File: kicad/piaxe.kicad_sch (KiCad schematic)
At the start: 13 parts, among them J3 Barrel_Jack_Switch, M2 Fan_4pin

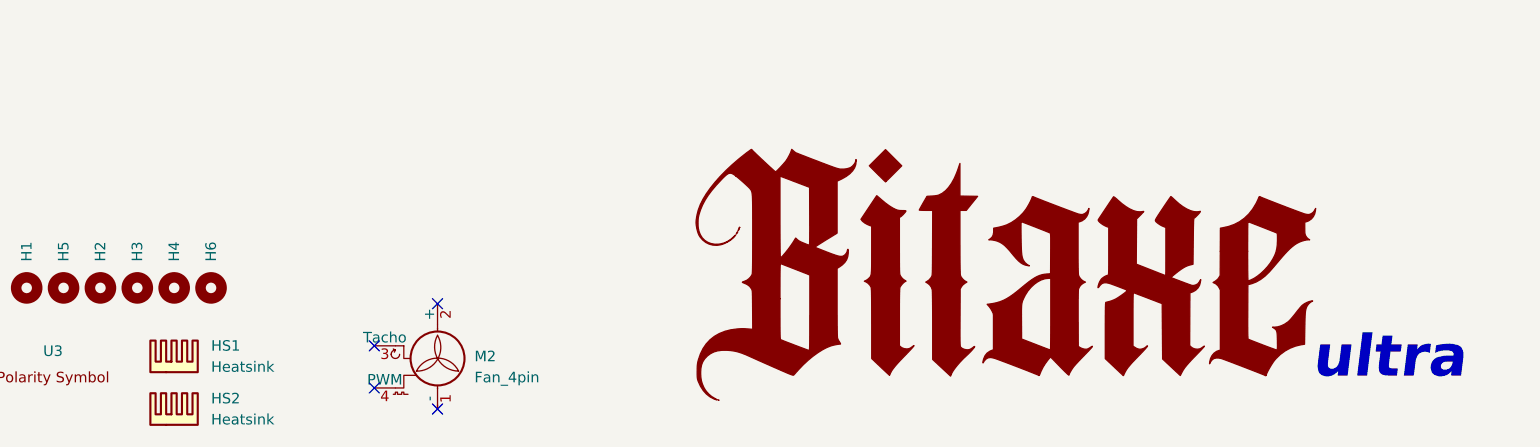
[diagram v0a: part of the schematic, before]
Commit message: fixed heatsink order number, updated BOM
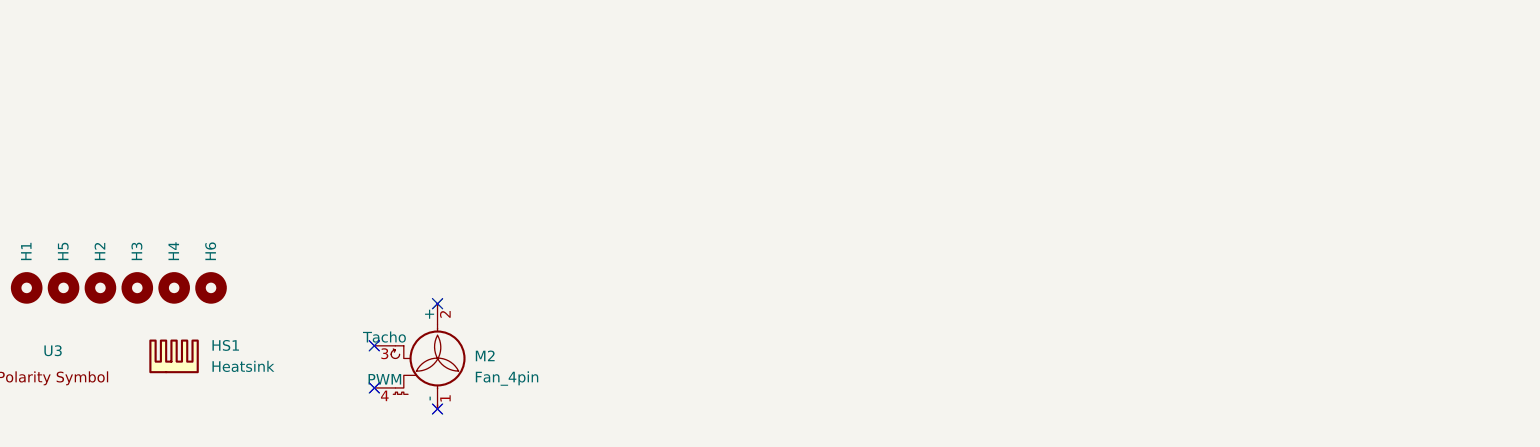
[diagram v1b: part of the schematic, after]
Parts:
- removed HS2: Heatsink, symbol Mechanical:Heatsink
- HS1: Manufacturer ATS-CPX040040025-184-C1-R0 -> ATS-CPX040040020-115-C1-R0; OrderNr ATS35997-ND -> ATS35987-ND
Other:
- note removed: "ultra"
- title: BM1366 bitaxe -> BM1366 PiAxe
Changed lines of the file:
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@@
   (paper "A")
   (title_block
-    (title "BM1366 bitaxe")
+    (title "BM1366 PiAxe")
     (date "2023-10-10")
     (rev "202")
@@
     (stroke (width 0) (type default))
   )
-  (text "ultra" (at 235.585 186.055 0)
-    (effects (font (size 5 5) (thickness 1) bold italic) (justify left bottom))
-  )
   (symbol (lib_id "Mechanical:MountingHole") (at 80.645 174.625 90) (unit 1)
     (in_bom yes) (on_board yes) (dnp no) (fields_autoplaced)
@@
     )
   )
-  (symbol (lib_id "bitaxe:LOGO") (at 197.485 173.99 0) (unit 1)
-    (in_bom yes) (on_board yes) (dnp no) (fields_autoplaced)
-    (property "Reference" "#G1" (at 197.485 146.4607 0)
-      (effects (font (size 1.27 1.27)) hide)
-    )
-    (property "Value" "LOGO" (at 197.485 201.5193 0)
-      (effects (font (size 1.27 1.27)) hide)
-    )
-    (property "Footprint" "" (at 197.485 173.99 0)
-      (effects (font (size 1.27 1.27)) hide)
-    )
-    (property "Datasheet" "" (at 197.485 173.99 0)
-      (effects (font (size 1.27 1.27)) hide)
-    )
-    (instances
-      (project "piaxe"
-        (path "/e63e39d7-6ac0-4ffd-8aa3-1841a4541b55"
-          (reference "#G1") (unit 1)
-        )
-      )
-    )
-  )
-  (symbol (lib_id "Mechanical:Heatsink") (at 98.425 191.135 0) (unit 1)
-    (in_bom yes) (on_board no) (dnp no) (fields_autoplaced)
-    (property "Reference" "HS2" (at 102.87 187.96 0)
-      (effects (font (size 1.27 1.27)) (justify left))
-    )
-    (property "Value" "Heatsink" (at 102.87 190.5 0)
-      (effects (font (size 1.27 1.27)) (justify left))
-    )
-    (property "Footprint" "" (at 98.7298 191.135 0)
-      (effects (font (size 1.27 1.27)) hide)
-    )
-    (property "Datasheet" "~" (at 98.7298 191.135 0)
-      (effects (font (size 1.27 1.27)) hide)
-    )
-    (property "Distributor" "D" (at 98.425 191.135 0)
-      (effects (font (size 1.27 1.27)) hide)
-    )
-    (property "Manufacturer" "ATS-FPX040040025-94-C2-R0" (at 98.425 191.135 0)
-      (effects (font (size 1.27 1.27)) hide)
-    )
-    (property "OrderNr" "ATS1674-ND" (at 98.425 191.135 0)
-      (effects (font (size 1.27 1.27)) hide)
-    )
-    (instances
-      (project "piaxe"
-        (path "/e63e39d7-6ac0-4ffd-8aa3-1841a4541b55"
-          (reference "HS2") (unit 1)
-        )
-      )
-    )
-  )
   (symbol (lib_id "bitaxe:polarity") (at 85.09 184.15 0) (unit 1)
     (in_bom no) (on_board yes) (dnp no) (fields_autoplaced)
@@
       (effects (font (size 1.27 1.27)) hide)
     )
-    (property "Manufacturer" "ATS-CPX040040025-184-C1-R0" (at 98.425 184.785 0)
-      (effects (font (size 1.27 1.27)) hide)
-    )
-    (property "OrderNr" "ATS35997-ND" (at 98.425 184.785 0)
-      (effects (font (size 1.27 1.27)) hide)
-    )
+    (property "Manufacturer" "ATS-CPX040040020-115-C1-R0" (at 98.425 184.785 0)
+      (effects (font (size 1.27 1.27)) hide)
+    )
+    (property "OrderNr" "ATS35987-ND" (at 98.425 184.785 0)
+      (effects (font (size 1.27 1.27)) hide)
+    )

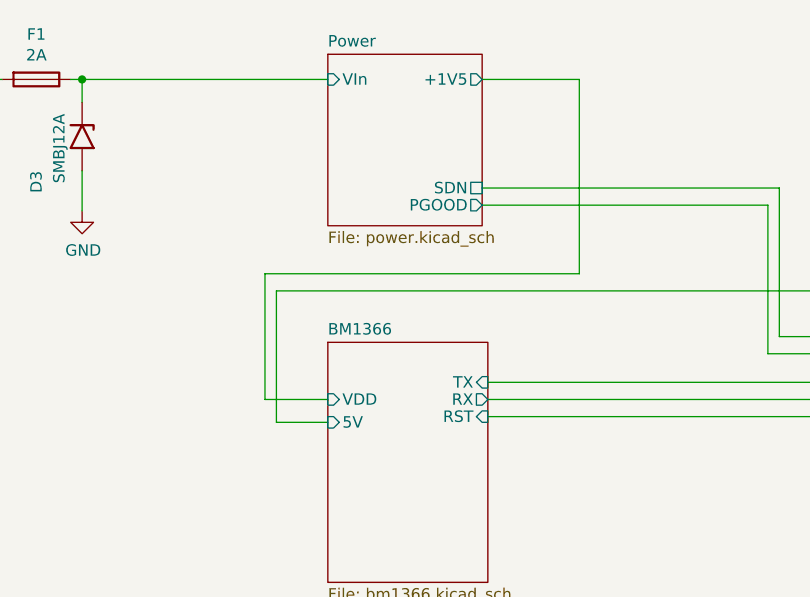
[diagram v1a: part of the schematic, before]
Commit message: fixed net labeling to 1.2V
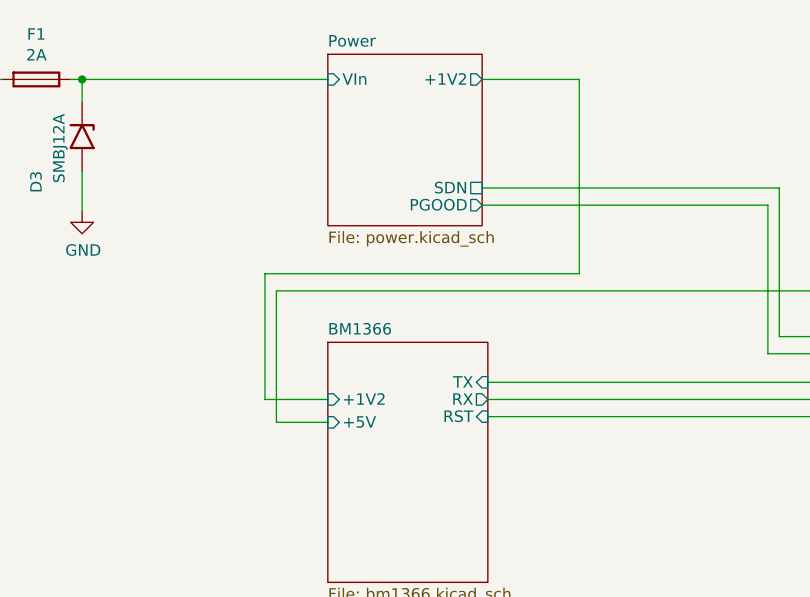
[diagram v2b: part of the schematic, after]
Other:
- sheet BM1366 ports: added +1V2, +5V; removed 5V, VDD
- sheet Power ports: added +1V2; removed +1V5
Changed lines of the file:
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@@
       (effects (font (size 1.27 1.27)) (justify right))
     )
-    (pin "5V" input (at 82.55 90.17 180)
+    (pin "+1V2" input (at 82.55 87.63 180)
       (effects (font (size 1.27 1.27)) (justify left))
     )
-    (pin "VDD" input (at 82.55 87.63 180)
+    (pin "+5V" input (at 82.55 90.17 180)
       (effects (font (size 1.27 1.27)) (justify left))
     )
@@
       (effects (font (size 1.27 1.27)) (justify right))
     )
-    (pin "+1V5" output (at 99.695 52.07 0)
-      (effects (font (size 1.27 1.27)) (justify right))
-    )
     (pin "SDN" passive (at 99.695 64.135 0)
       (effects (font (size 1.27 1.27)) (justify right))
@@
       (effects (font (size 1.27 1.27)) (justify left))
     )
+    (pin "+1V2" output (at 99.695 52.07 0)
+      (effects (font (size 1.27 1.27)) (justify right))
+    )
     (instances

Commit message: initial commit before replacing power supply
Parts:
- removed H1, H2, H3, H4, H5, H6: MountingHole, MountingHole:MountingHole_3.2mm_M3_DIN965_Pad, symbol Mechanical:MountingHole
- removed HS1: Heatsink, symbol Mechanical:Heatsink
- removed M2: Fan_4pin, symbol Motor:Fan_4pin
- renumbered U3 to U1
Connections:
- no-connect marks 4 -> 0
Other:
- sheet Power ports: added +0V8, +1V8, +3V3; removed none

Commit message: updated gerber, bom
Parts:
- F1: value 2A -> 5A; Manufacturer 0154002.DR -> 0154005.DR; OrderNr F1224CT-ND -> F1228CT-ND
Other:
- sheet Pi renamed STM32
- sheet BM1366 ports: added +0V8, +1V8, +3V3, RESET, RXD, TXD; removed +5V, RST, RX, TX
- sheet Power ports: added 1V2_PGOOD, 1V2_RUN; removed PGOOD, SDN
- sheet STM32 ports: added +3V3, 1V2_PGOOD, 1V2_RUN, RESET, RXD, TXD; removed +5V, BUCK_POWER_GOOD, BUCK_SHUTDOWN, MINER_RESET, MINER_RXD, MINER_TXD
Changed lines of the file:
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@@
     (rev "202")
   )
+  (junction (at 114.3 57.785) (diameter 0) (color 0 0 0 0)
+  )
   (junction (at 55.245 52.07) (diameter 0) (color 0 0 0 0)
   )
   (junction (at 43.815 57.15) (diameter 0) (color 0 0 0 0)
   )
-  (wire (pts (xy 110.49 73.66) (xy 75.565 73.66))
+  (wire (pts (xy 111.76 75.565) (xy 74.295 75.565))
+    (stroke (width 0) (type default))
+  )
+  (wire (pts (xy 74.295 75.565) (xy 74.295 89.535))
+    (stroke (width 0) (type default))
+  )
+  (wire (pts (xy 110.49 74.295) (xy 75.565 74.295))
     (stroke (width 0) (type default))
   )
@@
     (stroke (width 0) (type default))
   )
+  (wire (pts (xy 73.025 91.44) (xy 82.55 91.44))
+    (stroke (width 0) (type default))
+  )
   (wire (pts (xy 100.33 87.63) (xy 144.78 87.63))
     (stroke (width 0) (type default))
   )
+  (wire (pts (xy 73.025 76.835) (xy 73.025 91.44))
+    (stroke (width 0) (type default))
+  )
+  (wire (pts (xy 99.695 53.975) (xy 111.76 53.975))
+    (stroke (width 0) (type default))
+  )
   (wire (pts (xy 131.445 82.55) (xy 144.78 82.55))
     (stroke (width 0) (type default))
@@
     (stroke (width 0) (type default))
   )
+  (wire (pts (xy 71.755 78.105) (xy 71.755 93.345))
+    (stroke (width 0) (type default))
+  )
+  (wire (pts (xy 114.3 78.105) (xy 71.755 78.105))
+    (stroke (width 0) (type default))
+  )
   (wire (pts (xy 131.445 66.04) (xy 131.445 82.55))
     (stroke (width 0) (type default))
@@
     (stroke (width 0) (type default))
   )
-  (wire (pts (xy 110.49 52.07) (xy 110.49 73.66))
+  (wire (pts (xy 110.49 52.07) (xy 110.49 74.295))
     (stroke (width 0) (type default))
   )
@@
     (stroke (width 0) (type default))
   )
-  (wire (pts (xy 76.835 75.565) (xy 76.835 90.17))
+  (wire (pts (xy 71.755 93.345) (xy 82.55 93.345))
+    (stroke (width 0) (type default))
+  )
+  (wire (pts (xy 74.295 89.535) (xy 82.55 89.535))
+    (stroke (width 0) (type default))
+  )
+  (wire (pts (xy 144.78 78.74) (xy 133.985 78.74))
+    (stroke (width 0) (type default))
+  )
+  (wire (pts (xy 113.03 76.835) (xy 73.025 76.835))
+    (stroke (width 0) (type default))
+  )
+  (wire (pts (xy 133.985 78.74) (xy 133.985 57.785))
     (stroke (width 0) (type default))
   )
@@
     (stroke (width 0) (type default))
   )
-  (wire (pts (xy 144.78 75.565) (xy 76.835 75.565))
+  (wire (pts (xy 114.3 57.785) (xy 114.3 78.105))
     (stroke (width 0) (type default))
   )
@@
     (stroke (width 0) (type default))
   )
-  (wire (pts (xy 76.835 90.17) (xy 82.55 90.17))
-    (stroke (width 0) (type default))
-  )
   (wire (pts (xy 42.545 57.15) (xy 43.815 57.15))
     (stroke (width 0) (type default))
@@
     (stroke (width 0) (type default))
   )
+  (wire (pts (xy 113.03 55.88) (xy 113.03 76.835))
+    (stroke (width 0) (type default))
+  )
+  (wire (pts (xy 99.695 57.785) (xy 114.3 57.785))
+    (stroke (width 0) (type default))
+  )
+  (wire (pts (xy 133.985 57.785) (xy 114.3 57.785))
+    (stroke (width 0) (type default))
+  )
+  (wire (pts (xy 75.565 74.295) (xy 75.565 87.63))
+    (stroke (width 0) (type default))
+  )
+  (wire (pts (xy 99.695 55.88) (xy 113.03 55.88))
+    (stroke (width 0) (type default))
+  )
   (wire (pts (xy 100.33 85.725) (xy 144.78 85.725))
     (stroke (width 0) (type default))
@@
     (stroke (width 0) (type default))
   )
-  (wire (pts (xy 75.565 73.66) (xy 75.565 87.63))
-    (stroke (width 0) (type default))
-  )
   (wire (pts (xy 99.695 64.135) (xy 132.715 64.135))
+    (stroke (width 0) (type default))
+  )
+  (wire (pts (xy 111.76 53.975) (xy 111.76 75.565))
     (stroke (width 0) (type default))
   )
@@
       (effects (font (size 1.27 1.27)))
     )
-    (property "Value" "2A" (at 50.165 49.3776 90)
+    (property "Value" "5A" (at 50.165 49.3776 90)
       (effects (font (size 1.27 1.27)))
     )
@@
       (effects (font (size 1.27 1.27)) hide)
     )
-    (property "Manufacturer" "0154002.DR" (at 50.165 52.07 0)
-      (effects (font (size 1.27 1.27)) hide)
-    )
-    (property "OrderNr" "F1224CT-ND" (at 50.165 52.07 0)
+    (property "Manufacturer" "0154005.DR" (at 50.165 52.07 0)
+      (effects (font (size 1.27 1.27)) hide)
+    )
+    (property "OrderNr" "F1228CT-ND" (at 50.165 52.07 0)
       (effects (font (size 1.27 1.27)) hide)
     )
@@
       (effects (font (size 1.27 1.27)) (justify left top))
     )
-    (pin "TX" input (at 100.33 85.725 0)
-      (effects (font (size 1.27 1.27)) (justify right))
-    )
-    (pin "RX" output (at 100.33 87.63 0)
-      (effects (font (size 1.27 1.27)) (justify right))
-    )
-    (pin "RST" input (at 100.33 89.535 0)
-      (effects (font (size 1.27 1.27)) (justify right))
-    )
     (pin "+1V2" input (at 82.55 87.63 180)
       (effects (font (size 1.27 1.27)) (justify left))
     )
-    (pin "+5V" input (at 82.55 90.17 180)
-      (effects (font (size 1.27 1.27)) (justify left))
+    (pin "+1V8" input (at 82.55 89.535 180)
+      (effects (font (size 1.27 1.27)) (justify left))
+    )
+    (pin "+0V8" input (at 82.55 91.44 180)
+      (effects (font (size 1.27 1.27)) (justify left))
+    )
+    (pin "+3V3" input (at 82.55 93.345 180)
+      (effects (font (size 1.27 1.27)) (justify left))
+    )
+    (pin "RXD" output (at 100.33 87.63 0)
+      (effects (font (size 1.27 1.27)) (justify right))
+    )
+    (pin "TXD" input (at 100.33 85.725 0)
+      (effects (font (size 1.27 1.27)) (justify right))
+    )
+    (pin "RESET" input (at 100.33 89.535 0)
+      (effects (font (size 1.27 1.27)) (justify right))
     )
     (instances
@@
       (effects (font (size 1.27 1.27)) (justify left top))
     )
-    (pin "PGOOD" output (at 99.695 66.04 0)
-      (effects (font (size 1.27 1.27)) (justify right))
-    )
-    (pin "SDN" passive (at 99.695 64.135 0)
-      (effects (font (size 1.27 1.27)) (justify right))
-    )
     (pin "VIn" input (at 82.55 52.07 180)
       (effects (font (size 1.27 1.27)) (justify left))
@@
       (effects (font (size 1.27 1.27)) (justify right))
     )
-    (pin "+3V3" output (at 99.695 60.325 0)
+    (pin "+3V3" output (at 99.695 57.785 0)
       (effects (font (size 1.27 1.27)) (justify right))
     )
@@
     )
     (pin "+0V8" output (at 99.695 55.88 0)
+      (effects (font (size 1.27 1.27)) (justify right))
+    )
+    (pin "1V2_PGOOD" output (at 99.695 66.04 0)
+      (effects (font (size 1.27 1.27)) (justify right))
+    )
+    (pin "1V2_RUN" input (at 99.695 64.135 0)
       (effects (font (size 1.27 1.27)) (justify right))
     )
@@
     (stroke (width 0.1524) (type solid))
     (fill (color 255 255 194 1.0000))
-    (property "Sheetname" "Pi" (at 144.78 72.9484 0)
+    (property "Sheetname" "STM32" (at 144.78 72.9484 0)
       (effects (font (size 1.27 1.27)) (justify left bottom))
     )
@@
       (effects (font (size 1.27 1.27)) (justify left top))
     )
-    (pin "+5V" passive (at 144.78 75.565 180)
-      (effects (font (size 1.27 1.27)) (justify left))
-    )
-    (pin "MINER_TXD" output (at 144.78 85.725 180)
-      (effects (font (size 1.27 1.27)) (justify left))
-    )
-    (pin "MINER_RXD" input (at 144.78 87.63 180)
-      (effects (font (size 1.27 1.27)) (justify left))
-    )
-    (pin "BUCK_SHUTDOWN" output (at 144.78 80.645 180)
-      (effects (font (size 1.27 1.27)) (justify left))
-    )
-    (pin "BUCK_POWER_GOOD" input (at 144.78 82.55 180)
-      (effects (font (size 1.27 1.27)) (justify left))
-    )
-    (pin "MINER_RESET" output (at 144.78 89.535 180)
-      (effects (font (size 1.27 1.27)) (justify left))
-    )
+    (pin "1V2_RUN" output (at 144.78 80.645 180)
+      (effects (font (size 1.27 1.27)) (justify left))
+    )
+    (pin "+3V3" input (at 144.78 78.74 180)
+      (effects (font (size 1.27 1.27)) (justify left))
+    )
+    (pin "RXD" input (at 144.78 87.63 180)
+      (effects (font (size 1.27 1.27)) (justify left))
+    )
+    (pin "TXD" output (at 144.78 85.725 180)
+      (effects (font (size 1.27 1.27)) (justify left))
+    )
+    (pin "RESET" output (at 144.78 89.535 180)
+      (effects (font (size 1.27 1.27)) (justify left))
+    )
+    (pin "1V2_PGOOD" input (at 144.78 82.55 180)
+      (effects (font (size 1.27 1.27)) (justify left))
+    )
